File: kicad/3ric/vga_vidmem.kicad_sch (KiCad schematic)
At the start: 10 parts

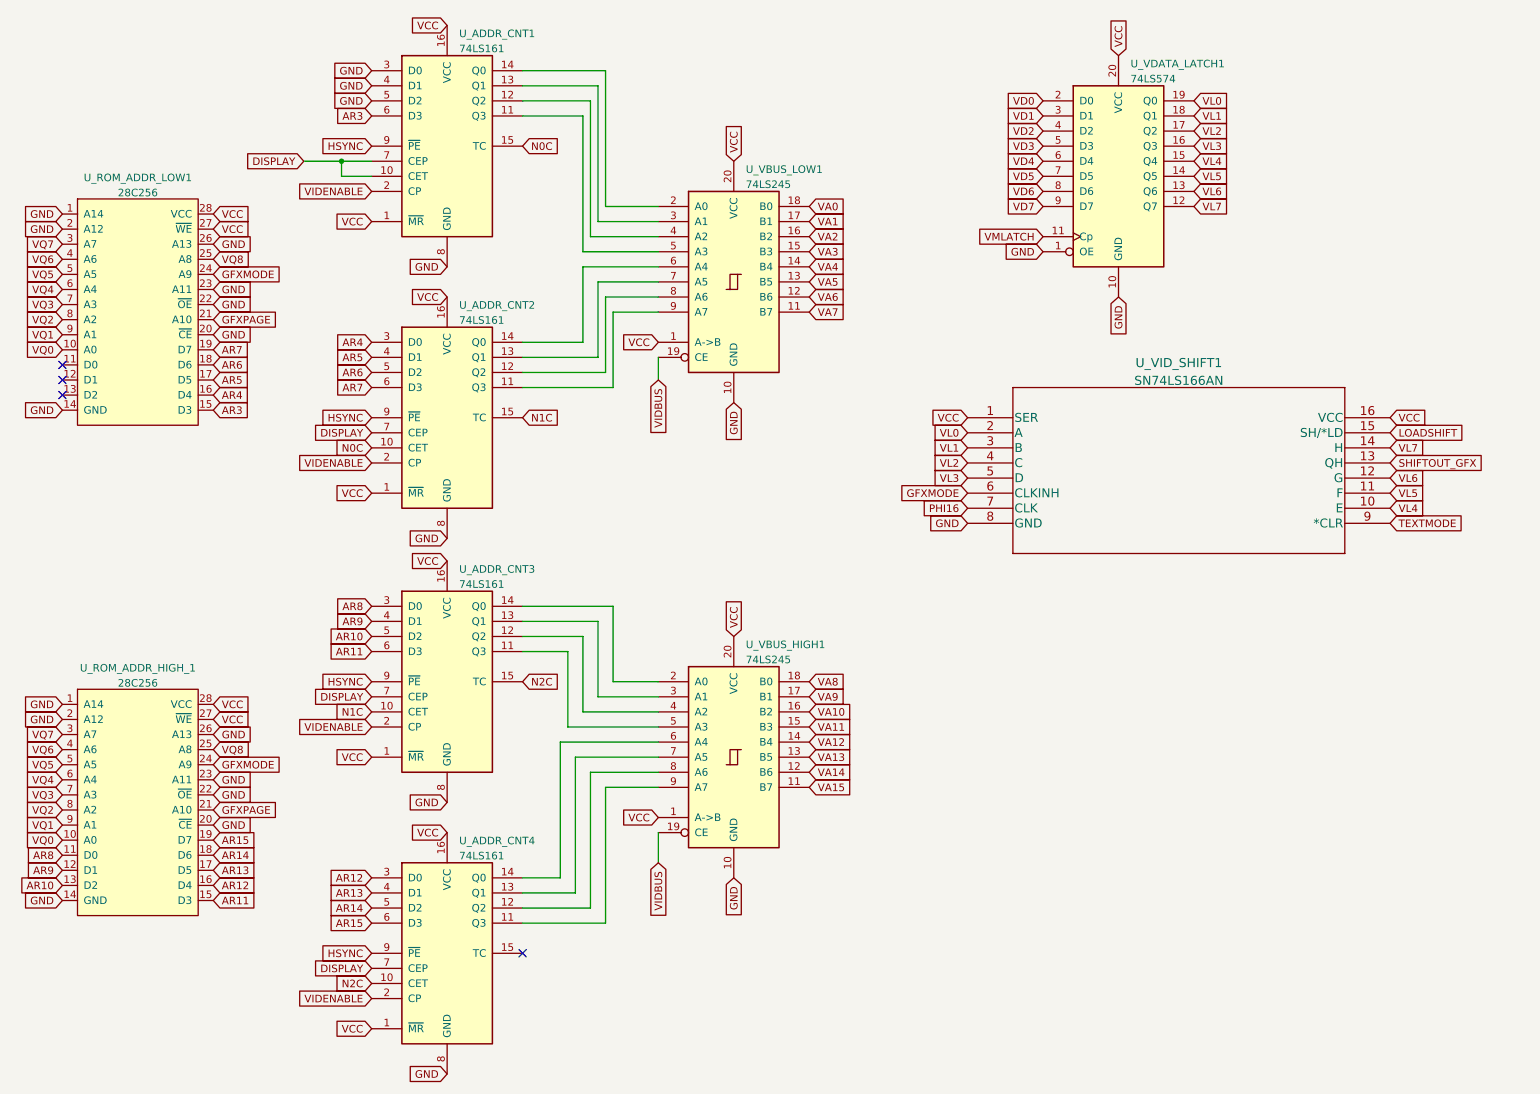
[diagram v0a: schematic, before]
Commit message: schematic updates - bring the schematics up to match breadboard changes current state has high res Apple II color emulation working
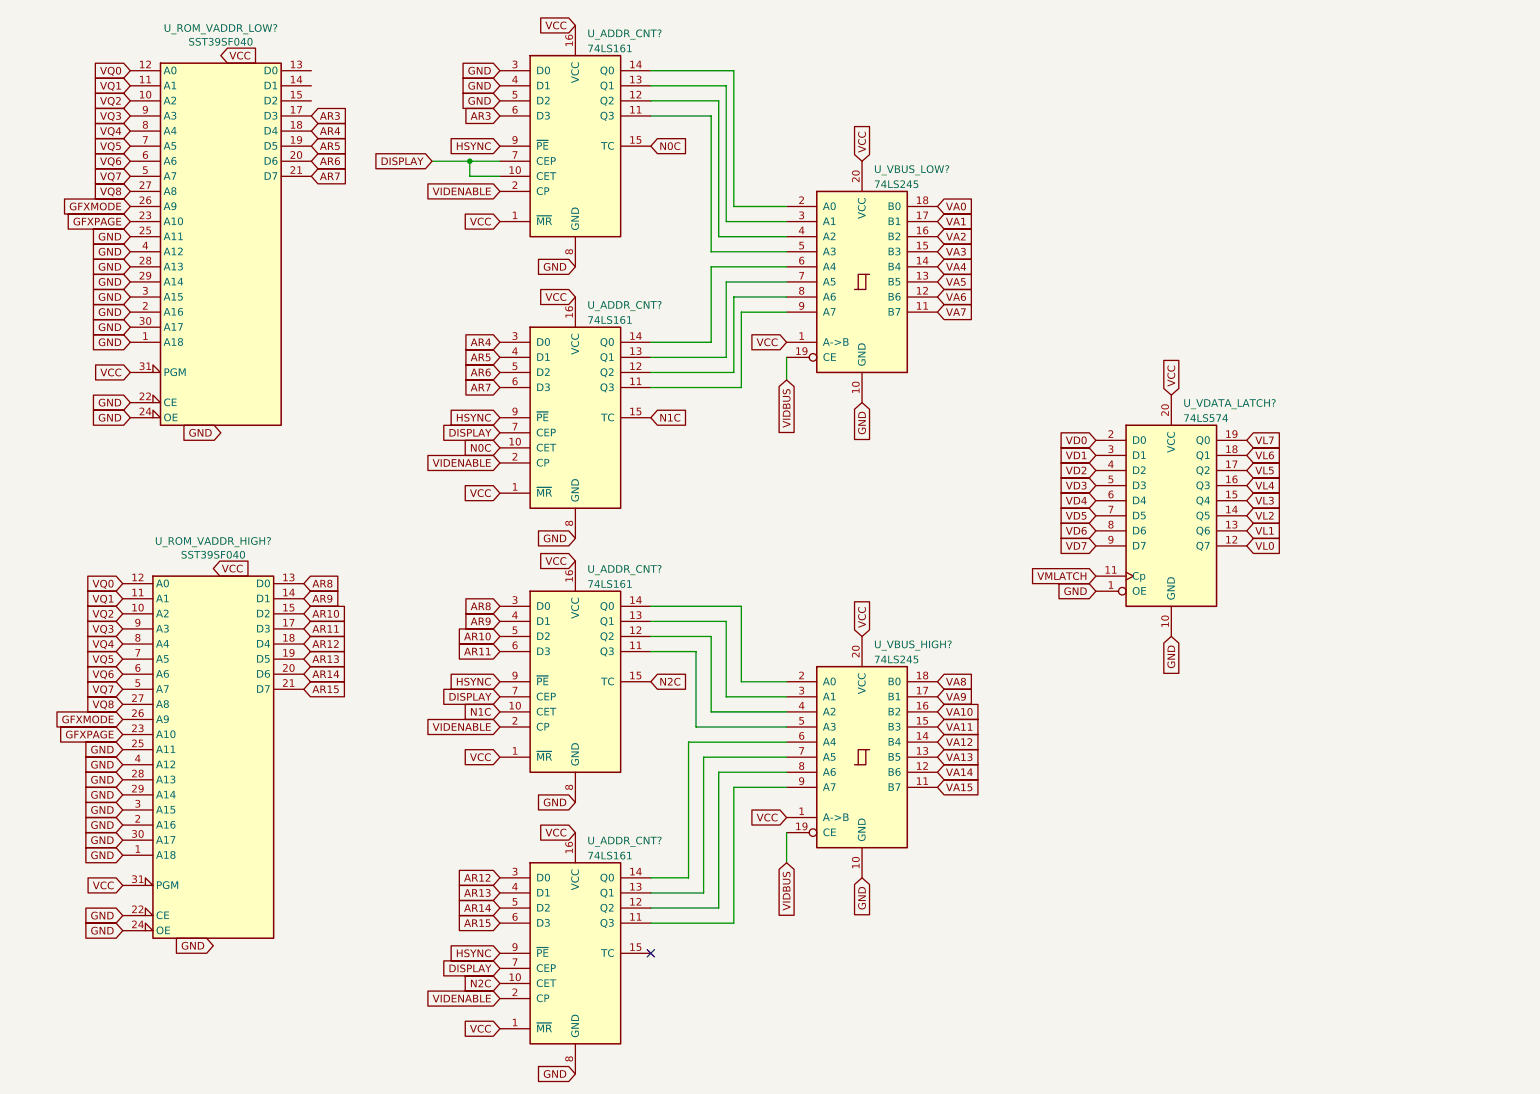
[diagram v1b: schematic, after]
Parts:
- removed U_ROM_ADDR_HIGH_1, U_ROM_ADDR_LOW1: 28C256, Package_DIP:DIP-28_W15.24mm_Socket, symbol 6502:28C256
- removed U_VID_SHIFT1: SN74LS166AN, Package_DIP:DIP-16_W7.62mm_Socket, symbol 74ls166:SN74LS166AN
- added U_ROM_VADDR_HIGH?, U_ROM_VADDR_LOW?: SST39SF040, Package_DIP:DIP-32_W15.24mm_Socket, symbol Memory_Flash:SST39SF040
- renumbered U_ADDR_CNT4 to U_ADDR_CNT?, U_ADDR_CNT1 to U_ADDR_CNT?, U_ADDR_CNT2 to U_ADDR_CNT?, U_ADDR_CNT3 to U_ADDR_CNT?, U_VBUS_HIGH1 to U_VBUS_HIGH?, U_VBUS_LOW1 to U_VBUS_LOW?, U_VDATA_LATCH1 to U_VDATA_LATCH?
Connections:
- net AR10: now also U_ROM_VADDR_HIGH?.15 (D2)
- net AR11: now also U_ROM_VADDR_HIGH?.17 (D3)
- net AR12: now also U_ROM_VADDR_HIGH?.18 (D4)
- net AR13: now also U_ROM_VADDR_HIGH?.19 (D5)
- net AR14: now also U_ROM_VADDR_HIGH?.20 (D6)
- net AR15: now also U_ROM_VADDR_HIGH?.21 (D7)
- net AR3: now also U_ROM_VADDR_LOW?.17 (D3)
- net AR4: now also U_ROM_VADDR_LOW?.18 (D4)
- net AR5: now also U_ROM_VADDR_LOW?.19 (D5)
- net AR6: now also U_ROM_VADDR_LOW?.20 (D6)
- net AR7: now also U_ROM_VADDR_LOW?.21 (D7)
- net AR8: now also U_ROM_VADDR_HIGH?.13 (D0)
- net AR9: now also U_ROM_VADDR_HIGH?.14 (D1)
- net GFXMODE: now also U_ROM_VADDR_HIGH?.26 (A9), U_ROM_VADDR_LOW?.26 (A9)
- net GFXPAGE: now also U_ROM_VADDR_HIGH?.23 (A10), U_ROM_VADDR_LOW?.23 (A10)
- net GND: now also U_ROM_VADDR_HIGH?.1 (A18), U_ROM_VADDR_HIGH?.16 (GND), U_ROM_VADDR_HIGH?.2 (A16), U_ROM_VADDR_HIGH?.22 (CE), U_ROM_VADDR_HIGH?.24 (OE), U_ROM_VADDR_HIGH?.25 (A11), U_ROM_VADDR_HIGH?.28 (A13), U_ROM_VADDR_HIGH?.29 (A14), U_ROM_VADDR_HIGH?.3 (A15), U_ROM_VADDR_HIGH?.30 (A17), U_ROM_VADDR_HIGH?.4 (A12), U_ROM_VADDR_LOW?.1 (A18), U_ROM_VADDR_LOW?.16 (GND), U_ROM_VADDR_LOW?.2 (A16), U_ROM_VADDR_LOW?.22 (CE), U_ROM_VADDR_LOW?.24 (OE), U_ROM_VADDR_LOW?.25 (A11), U_ROM_VADDR_LOW?.28 (A13), U_ROM_VADDR_LOW?.29 (A14), U_ROM_VADDR_LOW?.3 (A15), U_ROM_VADDR_LOW?.30 (A17), U_ROM_VADDR_LOW?.4 (A12)
- net VCC: now also U_ROM_VADDR_HIGH?.31 (PGM), U_ROM_VADDR_HIGH?.32 (VCC), U_ROM_VADDR_LOW?.31 (PGM), U_ROM_VADDR_LOW?.32 (VCC)
- net VL0: now also U_VDATA_LATCH?.12 (Q7); no longer U_VDATA_LATCH?.19 (Q0)
- net VL1: now also U_VDATA_LATCH?.13 (Q6); no longer U_VDATA_LATCH?.18 (Q1)
- net VL2: now also U_VDATA_LATCH?.14 (Q5); no longer U_VDATA_LATCH?.17 (Q2)
- net VL3: now also U_VDATA_LATCH?.15 (Q4); no longer U_VDATA_LATCH?.16 (Q3)
- net VL4: now also U_VDATA_LATCH?.16 (Q3); no longer U_VDATA_LATCH?.15 (Q4)
- net VL5: now also U_VDATA_LATCH?.17 (Q2); no longer U_VDATA_LATCH?.14 (Q5)
- net VL6: now also U_VDATA_LATCH?.18 (Q1); no longer U_VDATA_LATCH?.13 (Q6)
- net VL7: now also U_VDATA_LATCH?.19 (Q0); no longer U_VDATA_LATCH?.12 (Q7)
- net VQ0: now also U_ROM_VADDR_HIGH?.12 (A0), U_ROM_VADDR_LOW?.12 (A0)
- net VQ1: now also U_ROM_VADDR_HIGH?.11 (A1), U_ROM_VADDR_LOW?.11 (A1)
- net VQ2: now also U_ROM_VADDR_HIGH?.10 (A2), U_ROM_VADDR_LOW?.10 (A2)
- net VQ3: now also U_ROM_VADDR_HIGH?.9 (A3), U_ROM_VADDR_LOW?.9 (A3)
- net VQ4: now also U_ROM_VADDR_HIGH?.8 (A4), U_ROM_VADDR_LOW?.8 (A4)
- net VQ5: now also U_ROM_VADDR_HIGH?.7 (A5), U_ROM_VADDR_LOW?.7 (A5)
- net VQ6: now also U_ROM_VADDR_HIGH?.6 (A6), U_ROM_VADDR_LOW?.6 (A6)
- net VQ7: now also U_ROM_VADDR_HIGH?.5 (A7), U_ROM_VADDR_LOW?.5 (A7)
- net VQ8: now also U_ROM_VADDR_HIGH?.27 (A8), U_ROM_VADDR_LOW?.27 (A8)
- no-connect marks 4 -> 1
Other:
- moved on the sheet: U_ADDR_CNT?, U_VBUS_HIGH?, U_VBUS_LOW?, U_VDATA_LATCH?

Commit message: updates to logisim project and schematics
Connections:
- net GND: no longer U_ROM_VADDR_HIGH?.25 (A11), U_ROM_VADDR_HIGH?.4 (A12), U_ROM_VADDR_LOW?.25 (A11), U_ROM_VADDR_LOW?.4 (A12)
- net TEXTSHIFT: now reaches U_ROM_VADDR_LOW?.13 (D0)
- net GFXSHIFT: now reaches U_ROM_VADDR_LOW?.14 (D1)
- net GFXPAGE renamed PAGE1
- new net FULLMODE: U_ROM_VADDR_HIGH?.25 (A11), U_ROM_VADDR_LOW?.25 (A11)
- new net HIRES: U_ROM_VADDR_HIGH?.4 (A12), U_ROM_VADDR_LOW?.4 (A12)
- no-connect marks 1 -> 2
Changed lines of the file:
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@@
   )
   (no_connect (at 129.54 173.99))
+  (no_connect (at 72.39 30.48))
   (wire (pts (xy 143.51 76.2) (xy 143.51 63.5))
     (stroke (width 0) (type default) (color 0 0 0 0))
@@
     (stroke (width 0) (type default) (color 0 0 0 0))
   )
-  (wire (pts (xy 92.71 40.64) (xy 99.06 40.64))
+  (wire (pts (xy 93.98 40.64) (xy 99.06 40.64))
     (stroke (width 0) (type default) (color 0 0 0 0))
   )
@@
     )
   )
+  (global_label "HIRES" (shape input) (at 40.64 142.24 180) (fields_autoplaced)
+    (effects (font (size 1.27 1.27)) (justify right))
+    (property "Intersheet References" "${INTERSHEET_REFS}" (id 0) (at 32.6631 142.1606 0)
+      (effects (font (size 1.27 1.27)) (justify right) hide)
+    )
+  )
   (global_label "VQ1" (shape input) (at 41.91 27.94 180) (fields_autoplaced)
     (effects (font (size 1.27 1.27)) (justify right))
@@
     )
   )
+  (global_label "PAGE1" (shape input) (at 40.64 137.16 180) (fields_autoplaced)
+    (effects (font (size 1.27 1.27)) (justify right))
+    (property "Intersheet References" "${INTERSHEET_REFS}" (id 0) (at 32.2398 137.0806 0)
+      (effects (font (size 1.27 1.27)) (justify right) hide)
+    )
+  )
   (global_label "VD0" (shape input) (at 204.47 87.63 180) (fields_autoplaced)
     (effects (font (size 1.27 1.27)) (justify right))
@@
     )
   )
+  (global_label "TEXTSHIFT" (shape input) (at 72.39 25.4 0) (fields_autoplaced)
+    (effects (font (size 1.27 1.27)) (justify left))
+    (property "Intersheet References" "${INTERSHEET_REFS}" (id 0) (at 84.2979 25.3206 0)
+      (effects (font (size 1.27 1.27)) (justify left) hide)
+    )
+  )
   (global_label "VA3" (shape input) (at 177.8 55.88 0) (fields_autoplaced)
     (effects (font (size 1.27 1.27)) (justify left))
@@
     )
   )
-  (global_label "GFXPAGE" (shape input) (at 41.91 50.8 180) (fields_autoplaced)
-    (effects (font (size 1.27 1.27)) (justify right))
-    (property "Intersheet References" "${INTERSHEET_REFS}" (id 0) (at 31.1512 50.7206 0)
+  (global_label "PAGE1" (shape input) (at 41.91 50.8 180) (fields_autoplaced)
+    (effects (font (size 1.27 1.27)) (justify right))
+    (property "Intersheet References" "${INTERSHEET_REFS}" (id 0) (at 33.5098 50.7206 0)
       (effects (font (size 1.27 1.27)) (justify right) hide)
     )
@@
     )
   )
-  (global_label "GND" (shape input) (at 40.64 139.7 180) (fields_autoplaced)
-    (effects (font (size 1.27 1.27)) (justify right))
-    (property "Intersheet References" "${INTERSHEET_REFS}" (id 0) (at 34.3564 139.7794 0)
-      (effects (font (size 1.27 1.27)) (justify right) hide)
-    )
-  )
   (global_label "VQ2" (shape input) (at 41.91 30.48 180) (fields_autoplaced)
     (effects (font (size 1.27 1.27)) (justify right))
@@
     )
   )
+  (global_label "GFXSHIFT" (shape input) (at 72.39 27.94 0) (fields_autoplaced)
+    (effects (font (size 1.27 1.27)) (justify left))
+    (property "Intersheet References" "${INTERSHEET_REFS}" (id 0) (at 83.5721 27.8606 0)
+      (effects (font (size 1.27 1.27)) (justify left) hide)
+    )
+  )
   (global_label "VQ0" (shape input) (at 41.91 25.4 180) (fields_autoplaced)
     (effects (font (size 1.27 1.27)) (justify right))
@@
     )
   )
+  (global_label "GFXMODE" (shape input) (at 40.64 134.62 180) (fields_autoplaced)
+    (effects (font (size 1.27 1.27)) (justify right))
+    (property "Intersheet References" "${INTERSHEET_REFS}" (id 0) (at 29.4579 134.5406 0)
+      (effects (font (size 1.27 1.27)) (justify right) hide)
+    )
+  )
   (global_label "AR12" (shape input) (at 71.12 121.92 0) (fields_autoplaced)
     (effects (font (size 1.27 1.27)) (justify left))
@@
     )
   )
-  (global_label "GFXMODE" (shape input) (at 40.64 134.62 180) (fields_autoplaced)
-    (effects (font (size 1.27 1.27)) (justify right))
-    (property "Intersheet References" "${INTERSHEET_REFS}" (id 0) (at 29.4579 134.5406 0)
-      (effects (font (size 1.27 1.27)) (justify right) hide)
-    )
-  )
   (global_label "VCC" (shape input) (at 217.17 80.01 90) (fields_autoplaced)
     (effects (font (size 1.27 1.27)) (justify left))
@@
     )
   )
-  (global_label "GND" (shape input) (at 40.64 142.24 180) (fields_autoplaced)
-    (effects (font (size 1.27 1.27)) (justify right))
-    (property "Intersheet References" "${INTERSHEET_REFS}" (id 0) (at 34.3564 142.1606 0)
-      (effects (font (size 1.27 1.27)) (justify right) hide)
-    )
-  )
   (global_label "VMLATCH" (shape input) (at 204.47 110.49 180) (fields_autoplaced)
     (effects (font (size 1.27 1.27)) (justify right))
@@
     )
   )
-  (global_label "GFXPAGE" (shape input) (at 40.64 137.16 180) (fields_autoplaced)
-    (effects (font (size 1.27 1.27)) (justify right))
-    (property "Intersheet References" "${INTERSHEET_REFS}" (id 0) (at 29.8812 137.0806 0)
-      (effects (font (size 1.27 1.27)) (justify right) hide)
-    )
-  )
-  (global_label "GND" (shape input) (at 41.91 55.88 180) (fields_autoplaced)
-    (effects (font (size 1.27 1.27)) (justify right))
-    (property "Intersheet References" "${INTERSHEET_REFS}" (id 0) (at 35.6264 55.9594 0)
-      (effects (font (size 1.27 1.27)) (justify right) hide)
-    )
-  )
   (global_label "VA11" (shape input) (at 177.8 135.89 0) (fields_autoplaced)
     (effects (font (size 1.27 1.27)) (justify left))
@@
     )
   )
-  (global_label "GND" (shape input) (at 41.91 53.34 180) (fields_autoplaced)
-    (effects (font (size 1.27 1.27)) (justify right))
-    (property "Intersheet References" "${INTERSHEET_REFS}" (id 0) (at 35.6264 53.4194 0)
+  (global_label "FULLMODE" (shape input) (at 41.91 53.34 180) (fields_autoplaced)
+    (effects (font (size 1.27 1.27)) (justify right))
+    (property "Intersheet References" "${INTERSHEET_REFS}" (id 0) (at 29.8207 53.2606 0)
       (effects (font (size 1.27 1.27)) (justify right) hide)
     )
@@
     )
   )
-  (global_label "DISPLAY" (shape input) (at 92.71 40.64 180) (fields_autoplaced)
-    (effects (font (size 1.27 1.27)) (justify right))
-    (property "Intersheet References" "${INTERSHEET_REFS}" (id 0) (at 82.7374 40.5606 0)
+  (global_label "DISPLAY" (shape input) (at 93.98 40.64 180) (fields_autoplaced)
+    (effects (font (size 1.27 1.27)) (justify right))
+    (property "Intersheet References" "${INTERSHEET_REFS}" (id 0) (at 84.0074 40.5606 0)
       (effects (font (size 1.27 1.27)) (justify right) hide)
     )
@@
     )
   )
+  (global_label "HIRES" (shape input) (at 41.91 55.88 180) (fields_autoplaced)
+    (effects (font (size 1.27 1.27)) (justify right))
+    (property "Intersheet References" "${INTERSHEET_REFS}" (id 0) (at 33.9331 55.8006 0)
+      (effects (font (size 1.27 1.27)) (justify right) hide)
+    )
+  )
   (global_label "VCC" (shape input) (at 165.1 40.64 90) (fields_autoplaced)
     (effects (font (size 1.27 1.27)) (justify left))
@@
     )
   )
+  (global_label "FULLMODE" (shape input) (at 40.64 139.7 180) (fields_autoplaced)
+    (effects (font (size 1.27 1.27)) (justify right))
+    (property "Intersheet References" "${INTERSHEET_REFS}" (id 0) (at 28.5507 139.6206 0)
+      (effects (font (size 1.27 1.27)) (justify right) hide)
+    )
+  )

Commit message: push schematic updates
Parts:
- removed U_VBUS_HIGH?, U_VBUS_LOW?: 74LS245, Package_DIP:DIP-20_W7.62mm_Socket, symbol 74xx:74LS245
- removed U_VDATA_LATCH?: 74LS574, Package_DIP:DIP-20_W7.62mm_Socket, symbol 74xx:74LS574
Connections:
- net XA8: now reaches U_ADDR_CNT?.14 (Q0)
- net XA9: now reaches U_ADDR_CNT?.13 (Q1)
- net XA10: now reaches U_ADDR_CNT?.12 (Q2)
- net XA11: now reaches U_ADDR_CNT?.11 (Q3)
- net XA12: now reaches U_ADDR_CNT?.14 (Q0)
- net XA13: now reaches U_ADDR_CNT?.13 (Q1)
- net XA14: now reaches U_ADDR_CNT?.12 (Q2)
- net XA15: now reaches U_ADDR_CNT?.11 (Q3)
- net XA0: now reaches U_ADDR_CNT?.14 (Q0)
- net XA1: now reaches U_ADDR_CNT?.13 (Q1)
- net XA2: now reaches U_ADDR_CNT?.12 (Q2)
- net XA3: now reaches U_ADDR_CNT?.11 (Q3)
- net XA4: now reaches U_ADDR_CNT?.14 (Q0)
- net XA5: now reaches U_ADDR_CNT?.13 (Q1)
- net XA6: now reaches U_ADDR_CNT?.12 (Q2)
- net XA7: now reaches U_ADDR_CNT?.11 (Q3)
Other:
- moved on the sheet: U_ADDR_CNT?, U_ROM_VADDR_HIGH?, U_ROM_VADDR_LOW?
